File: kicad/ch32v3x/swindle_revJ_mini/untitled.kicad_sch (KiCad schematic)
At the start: 8 parts, among them J1 jtag, J10 Debug port, J3 Dbg, J5 Debug port, J6 Debug port, J7 Conn_01x03_Pin, J8 Debug port, J9 Conn_01x03_Pin

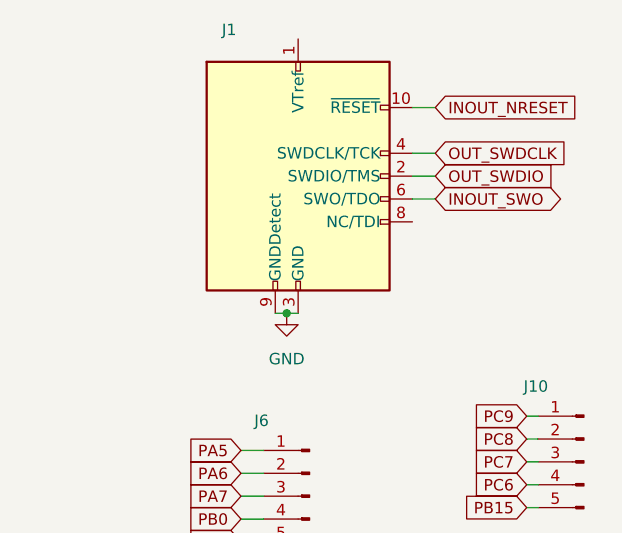
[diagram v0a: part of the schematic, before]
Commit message: add a WS2812b to the mini version, mini version for CH32,GD32 and RP2xxx
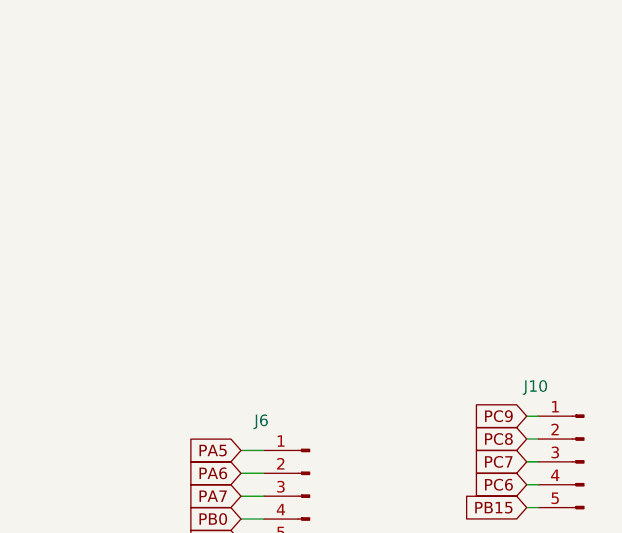
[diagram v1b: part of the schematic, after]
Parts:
- removed J1: jtag, Connector_PinHeader_1.27mm:PinHeader_2x05_P1.27mm_Vertical_SMD, symbol Connector:Conn_ARM_JTAG_SWD_10
